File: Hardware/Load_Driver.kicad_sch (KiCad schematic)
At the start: 4 parts, among them J1 VCF4-1000, J2 VCF4-1000

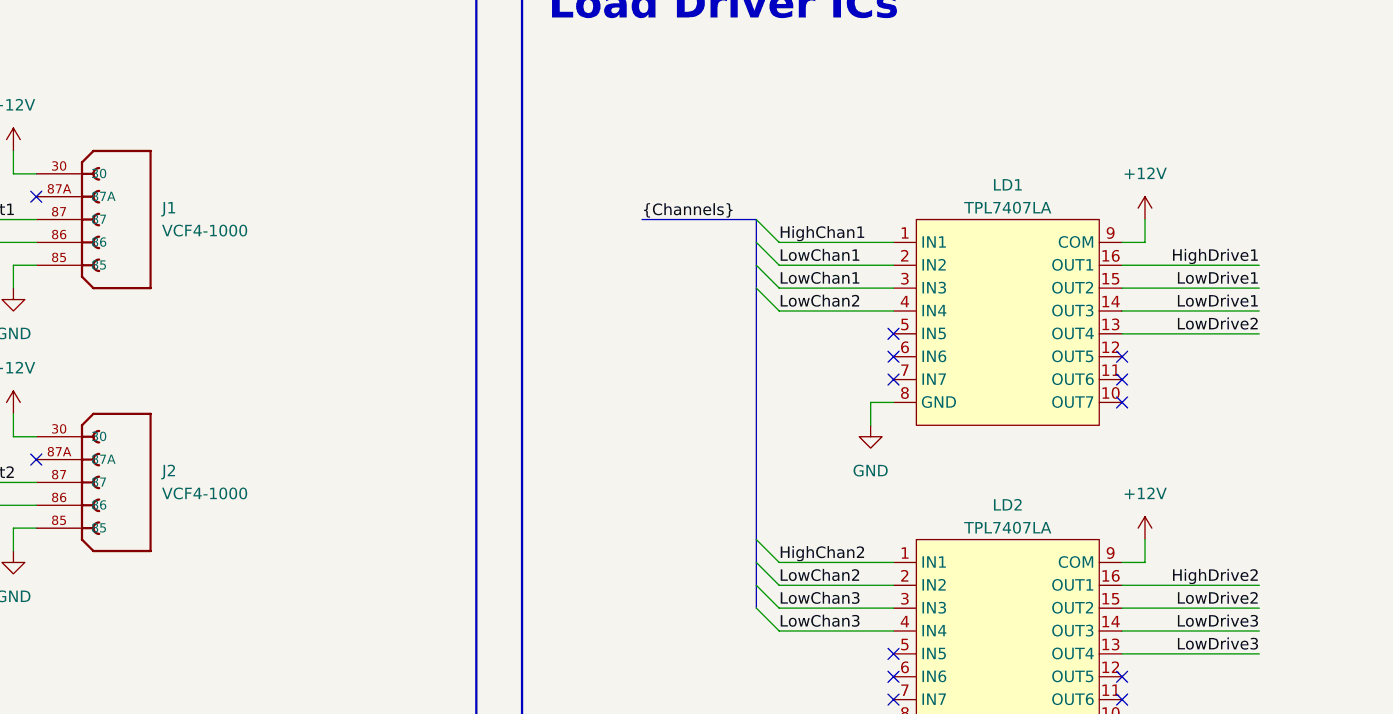
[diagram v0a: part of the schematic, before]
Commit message: Fixed up the schematic a little, and did *most* footprint assigning
- Most footprints are assigned. Ones that arent either don't exist, or
  are out of stock at digikey and are thus not work making/adding.
- Details of next steps will be put into changelog soon
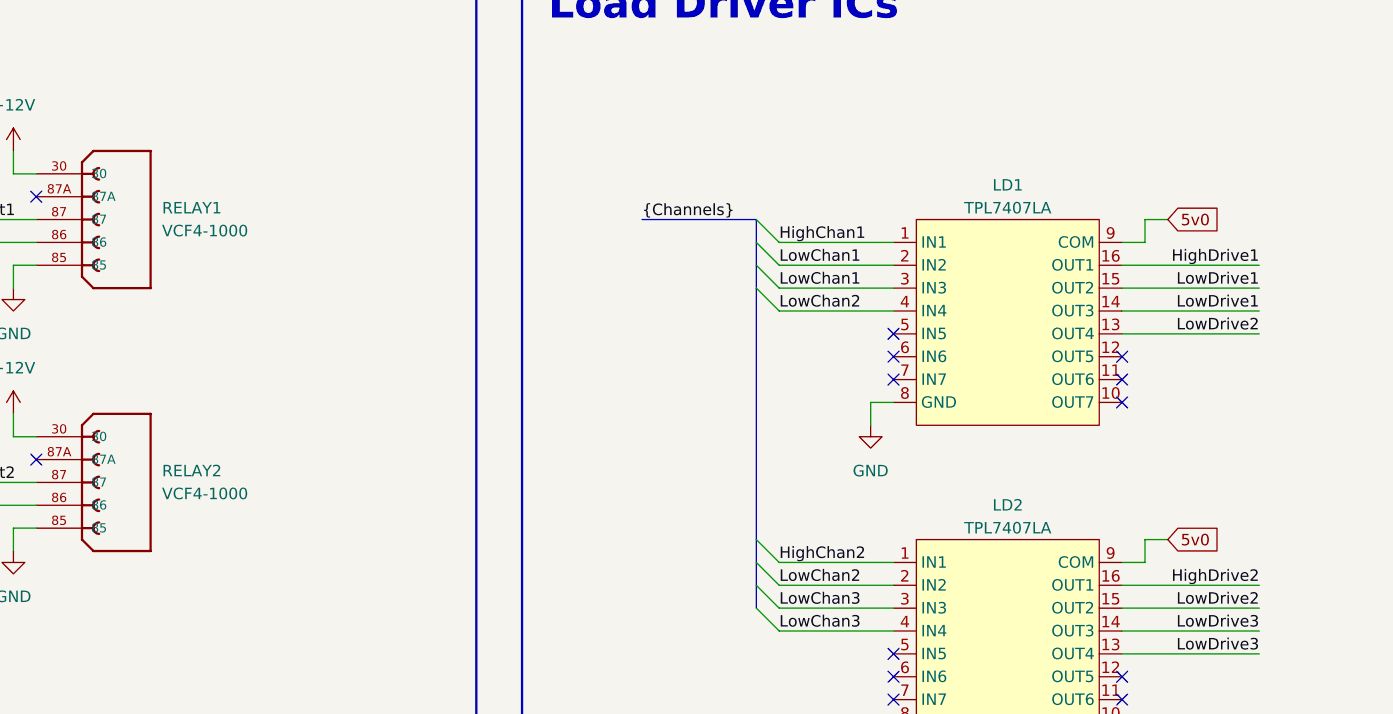
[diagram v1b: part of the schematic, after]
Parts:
- LD1, LD2: footprint (none) -> Package_SO:SOIC-16_3.9x9.9mm_P1.27mm
- RELAY1: renamed from J1; footprint VCF4-1000:TE_VCF4-1000 -> footprints:TE_VCF4-1000
- RELAY2: renamed from J2; footprint VCF4-1000:TE_VCF4-1000 -> footprints:TE_VCF4-1000
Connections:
- net +12V: no longer LD1.9 (COM), LD2.9 (COM)
- new net 5v0: LD1.9 (COM), LD2.9 (COM)
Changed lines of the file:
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@@
+	(wire
+		(pts
+			(xy 228.6 78.74) (xy 231.14 78.74)
+		)
+		(stroke
+			(width 0)
+			(type default)
+		)
+	)
 	(wire
 		(pts
@@
 		(pts
 			(xy 228.6 45.72) (xy 226.06 45.72)
+		)
+		(stroke
+			(width 0)
+			(type default)
+		)
+	)
+	(wire
+		(pts
+			(xy 228.6 43.18) (xy 231.14 43.18)
 		)
 		(stroke
@@
 		)
 	)
+	(global_label "5v0"
+		(shape input)
+		(at 231.14 78.74 0)
+		(fields_autoplaced yes)
+		(effects
+			(font
+				(size 1.27 1.27)
+			)
+			(justify left)
+		)
+		(property "Intersheetrefs" "${INTERSHEET_REFS}"
+			(at 237.5118 78.74 0)
+			(effects
+				(font
+					(size 1.27 1.27)
+				)
+				(justify left)
+				(hide yes)
+			)
+		)
+	)
+	(global_label "5v0"
+		(shape input)
+		(at 231.14 43.18 0)
+		(fields_autoplaced yes)
+		(effects
+			(font
+				(size 1.27 1.27)
+			)
+			(justify left)
+		)
+		(property "Intersheetrefs" "${INTERSHEET_REFS}"
+			(at 237.5118 43.18 0)
+			(effects
+				(font
+					(size 1.27 1.27)
+				)
+				(justify left)
+				(hide yes)
+			)
+		)
+	)
 	(hierarchical_label "{Channels}"
 		(shape input)
@@
 		(dnp no)
 		(fields_autoplaced yes)
-		(property "Reference" "#PWR010"
+		(property "Reference" "#PWR015"
 			(at 102.87 68.58 0)
 			(effects
@@
 			(project "CANIO-Board"
 				(path "/a11f98b2-3b09-4cf9-8535-19e509fe91b9/2ac81ea5-d7e0-4ba7-9177-0b729c928fc7"
-					(reference "#PWR010")
+					(reference "#PWR015")
 					(unit 1)
 				)
@@
 		(dnp no)
 		(fields_autoplaced yes)
-		(property "Reference" "#PWR05"
+		(property "Reference" "#PWR018"
 			(at 198.12 107.95 0)
 			(effects
@@
 			(project "CANIO-Board"
 				(path "/a11f98b2-3b09-4cf9-8535-19e509fe91b9/2ac81ea5-d7e0-4ba7-9177-0b729c928fc7"
-					(reference "#PWR05")
+					(reference "#PWR018")
 					(unit 1)
 				)
@@
 		(dnp no)
 		(fields_autoplaced yes)
-		(property "Reference" "J1"
+		(property "Reference" "RELAY1"
 			(at 119.38 41.9099 0)
 			(effects
@@
 			)
 		)
-		(property "Footprint" "VCF4-1000:TE_VCF4-1000"
+		(property "Footprint" "footprints:TE_VCF4-1000"
 			(at 110.49 43.18 0)
 			(effects
@@
 			(project ""
 				(path "/a11f98b2-3b09-4cf9-8535-19e509fe91b9/2ac81ea5-d7e0-4ba7-9177-0b729c928fc7"
-					(reference "J1")
-					(unit 1)
-				)
-			)
-		)
-	)
-	(symbol
-		(lib_id "power:+12V")
-		(at 228.6 78.74 0)
-		(unit 1)
-		(exclude_from_sim no)
-		(in_bom yes)
-		(on_board yes)
-		(dnp no)
-		(fields_autoplaced yes)
-		(property "Reference" "#PWR06"
-			(at 228.6 82.55 0)
-			(effects
-				(font
-					(size 1.27 1.27)
-				)
-				(hide yes)
-			)
-		)
-		(property "Value" "+12V"
-			(at 228.6 73.66 0)
-			(effects
-				(font
-					(size 1.27 1.27)
-				)
-			)
-		)
-		(property "Footprint" ""
-			(at 228.6 78.74 0)
-			(effects
-				(font
-					(size 1.27 1.27)
-				)
-				(hide yes)
-			)
-		)
-		(property "Datasheet" ""
-			(at 228.6 78.74 0)
-			(effects
-				(font
-					(size 1.27 1.27)
-				)
-				(hide yes)
-			)
-		)
-		(property "Description" "Power symbol creates a global label with name \"+12V\""
-			(at 228.6 78.74 0)
-			(effects
-				(font
-					(size 1.27 1.27)
-				)
-				(hide yes)
-			)
-		)
-		(pin "1"
-		)
-		(instances
-			(project "CANIO-Board"
-				(path "/a11f98b2-3b09-4cf9-8535-19e509fe91b9/2ac81ea5-d7e0-4ba7-9177-0b729c928fc7"
-					(reference "#PWR06")
+					(reference "RELAY1")
 					(unit 1)
 				)
@@
 		(dnp no)
 		(fields_autoplaced yes)
-		(property "Reference" "#PWR09"
+		(property "Reference" "#PWR013"
 			(at 102.87 39.37 0)
 			(effects
@@
 			(project ""
 				(path "/a11f98b2-3b09-4cf9-8535-19e509fe91b9/2ac81ea5-d7e0-4ba7-9177-0b729c928fc7"
-					(reference "#PWR09")
+					(reference "#PWR013")
 					(unit 1)
 				)
@@
 			)
 		)
-		(property "Footprint" ""
+		(property "Footprint" "Package_SO:SOIC-16_3.9x9.9mm_P1.27mm"
 			(at 213.36 53.34 0)
 			(effects
@@
 		(dnp no)
 		(fields_autoplaced yes)
-		(property "Reference" "#PWR08"
+		(property "Reference" "#PWR014"
 			(at 102.87 57.15 0)
 			(effects
@@
 			(project "CANIO-Board"
 				(path "/a11f98b2-3b09-4cf9-8535-19e509fe91b9/2ac81ea5-d7e0-4ba7-9177-0b729c928fc7"
-					(reference "#PWR08")
+					(reference "#PWR014")
 					(unit 1)
 				)
@@
 		(dnp no)
 		(fields_autoplaced yes)
-		(property "Reference" "#PWR07"
+		(property "Reference" "#PWR016"
 			(at 102.87 86.36 0)
 			(effects
@@
 			(project "CANIO-Board"
 				(path "/a11f98b2-3b09-4cf9-8535-19e509fe91b9/2ac81ea5-d7e0-4ba7-9177-0b729c928fc7"
-					(reference "#PWR07")
+					(reference "#PWR016")
 					(unit 1)
 				)
@@
 			)
 		)
-		(property "Footprint" ""
+		(property "Footprint" "Package_SO:SOIC-16_3.9x9.9mm_P1.27mm"
 			(at 213.36 88.9 0)
 			(effects
@@
 		(dnp no)
 		(fields_autoplaced yes)
-		(property "Reference" "#PWR03"
+		(property "Reference" "#PWR017"
 			(at 198.12 72.39 0)
 			(effects
@@
 			(project ""
 				(path "/a11f98b2-3b09-4cf9-8535-19e509fe91b9/2ac81ea5-d7e0-4ba7-9177-0b729c928fc7"
-					(reference "#PWR03")
-					(unit 1)
-				)
-			)
-		)
-	)
-	(symbol
-		(lib_id "power:+12V")
-		(at 228.6 43.18 0)
-		(unit 1)
-		(exclude_from_sim no)
-		(in_bom yes)
-		(on_board yes)
-		(dnp no)
-		(fields_autoplaced yes)
-		(property "Reference" "#PWR04"
-			(at 228.6 46.99 0)
-			(effects
-				(font
-					(size 1.27 1.27)
-				)
-				(hide yes)
-			)
-		)
-		(property "Value" "+12V"
-			(at 228.6 38.1 0)
-			(effects
-				(font
-					(size 1.27 1.27)
-				)
-			)
-		)
-		(property "Footprint" ""
-			(at 228.6 43.18 0)
-			(effects
-				(font
-					(size 1.27 1.27)
-				)
-				(hide yes)
-			)
-		)
-		(property "Datasheet" ""
-			(at 228.6 43.18 0)
-			(effects
-				(font
-					(size 1.27 1.27)
-				)
-				(hide yes)
-			)
-		)
-		(property "Description" "Power symbol creates a global label with name \"+12V\""
-			(at 228.6 43.18 0)
-			(effects
-				(font
-					(size 1.27 1.27)
-				)
-				(hide yes)
-			)
-		)
-		(pin "1"
-		)
-		(instances
-			(project ""
-				(path "/a11f98b2-3b09-4cf9-8535-19e509fe91b9/2ac81ea5-d7e0-4ba7-9177-0b729c928fc7"
-					(reference "#PWR04")
+					(reference "#PWR017")
 					(unit 1)
 				)
@@
 		(dnp no)
 		(fields_autoplaced yes)
-		(property "Reference" "J2"
+		(property "Reference" "RELAY2"
 			(at 119.38 71.1199 0)
 			(effects
@@
 			)
 		)
-		(property "Footprint" "VCF4-1000:TE_VCF4-1000"
+		(property "Footprint" "footprints:TE_VCF4-1000"
 			(at 110.49 72.39 0)
 			(effects
@@
 			(project "CANIO-Board"
 				(path "/a11f98b2-3b09-4cf9-8535-19e509fe91b9/2ac81ea5-d7e0-4ba7-9177-0b729c928fc7"
-					(reference "J2")
+					(reference "RELAY2")
 					(unit 1)
 				)
